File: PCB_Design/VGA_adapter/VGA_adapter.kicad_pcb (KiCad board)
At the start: 2 copper layers, 62.2 x 44.5 mm, 2 parts, among them J1 VGA Output, J2 PIC24 Curiosity Board Adapter

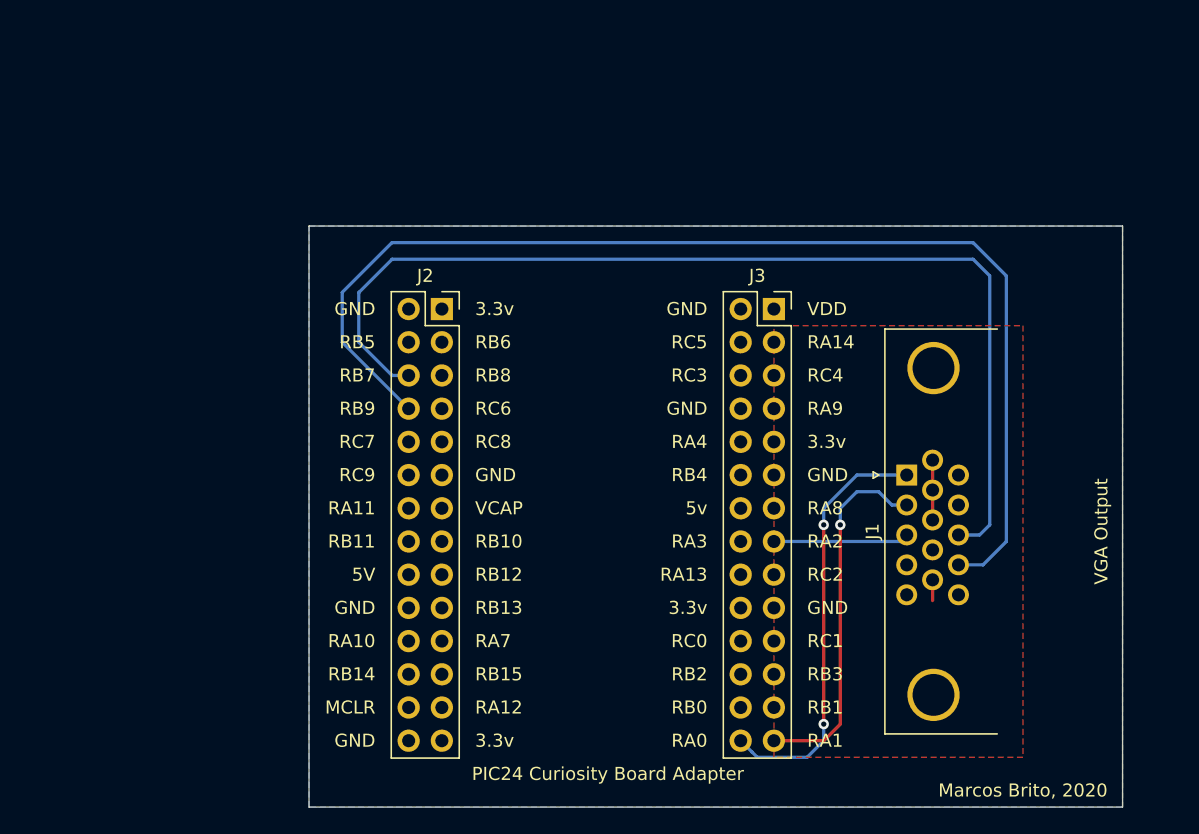
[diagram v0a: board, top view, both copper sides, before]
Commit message: First version of PCB adapter
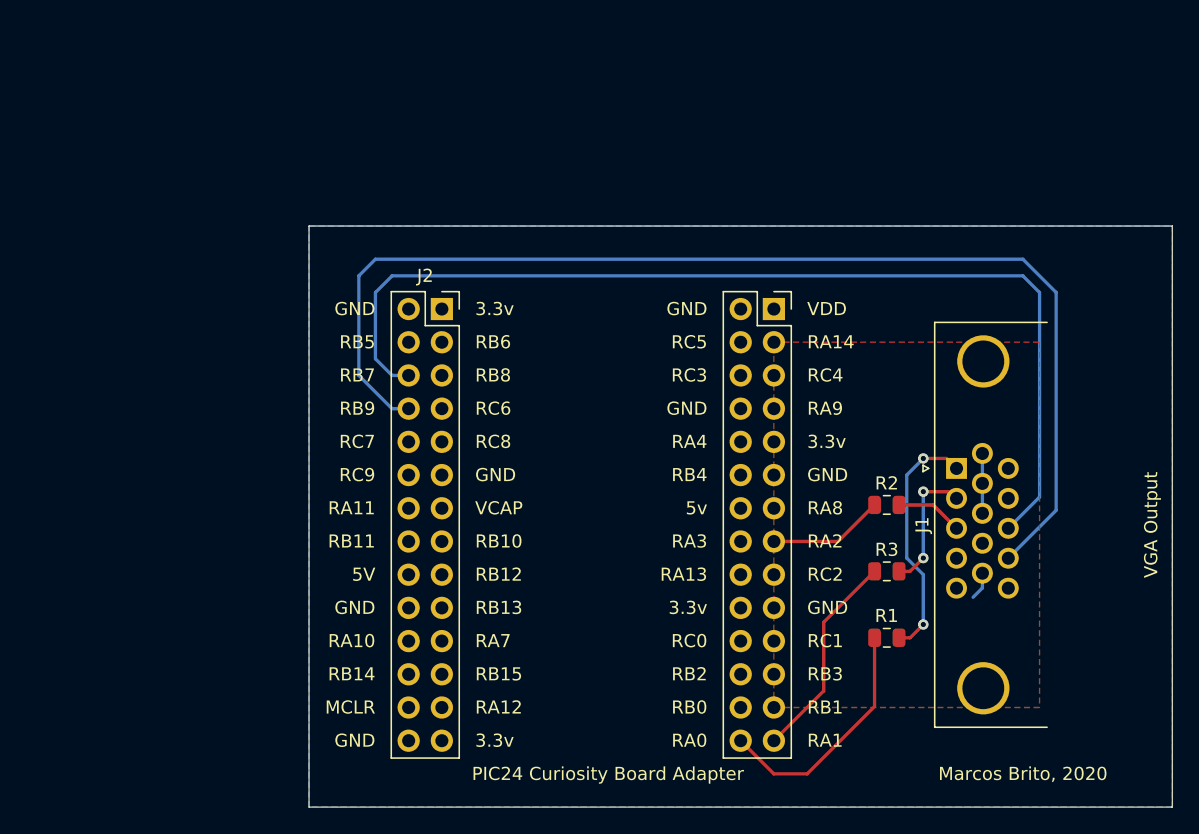
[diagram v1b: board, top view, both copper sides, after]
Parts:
- added R1: 470, Resistor_SMD:R_0805_2012Metric, F.Cu at (171.2, 109.0)
- added R2: 470, Resistor_SMD:R_0805_2012Metric, F.Cu at (171.2, 98.8)
- added R3: 470, Resistor_SMD:R_0805_2012Metric, F.Cu at (171.2, 103.9)
- moved J1 3.84 mm to (176.5, 96.0)
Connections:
- J1 pad 11: Net-(J1-Pad11) -> (no net)
- J2 pad 43: BLUE -> Net-(J2-Pad43)
- J2 pad 55: GREEN -> Net-(J2-Pad55)
- J2 pad 56: RED -> Net-(J2-Pad56)
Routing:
- net Net-(J2-Pad56): track 0.00 -> 18.7 mm
- net GREEN: track 28.1 -> 10.1 mm, vias 1 -> 2
- net Net-(J2-Pad55): track 0.00 -> 16.1 mm
- net RED: track 32.6 -> 18.9 mm
- net Net-(J2-Pad43): track 0.00 -> 8.86 mm
- net BLUE: track 10.4 -> 5.14 mm
- net H_SYNC: track 80.3 -> 79.0 mm
- net GND: track 6.17 -> 6.72 mm
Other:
- board size 62.2 x 44.5 mm -> 66 x 44.5 mm
- board text removed: "J3"

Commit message: PCB_Design: Add resistors to .sch and 3D model for pins
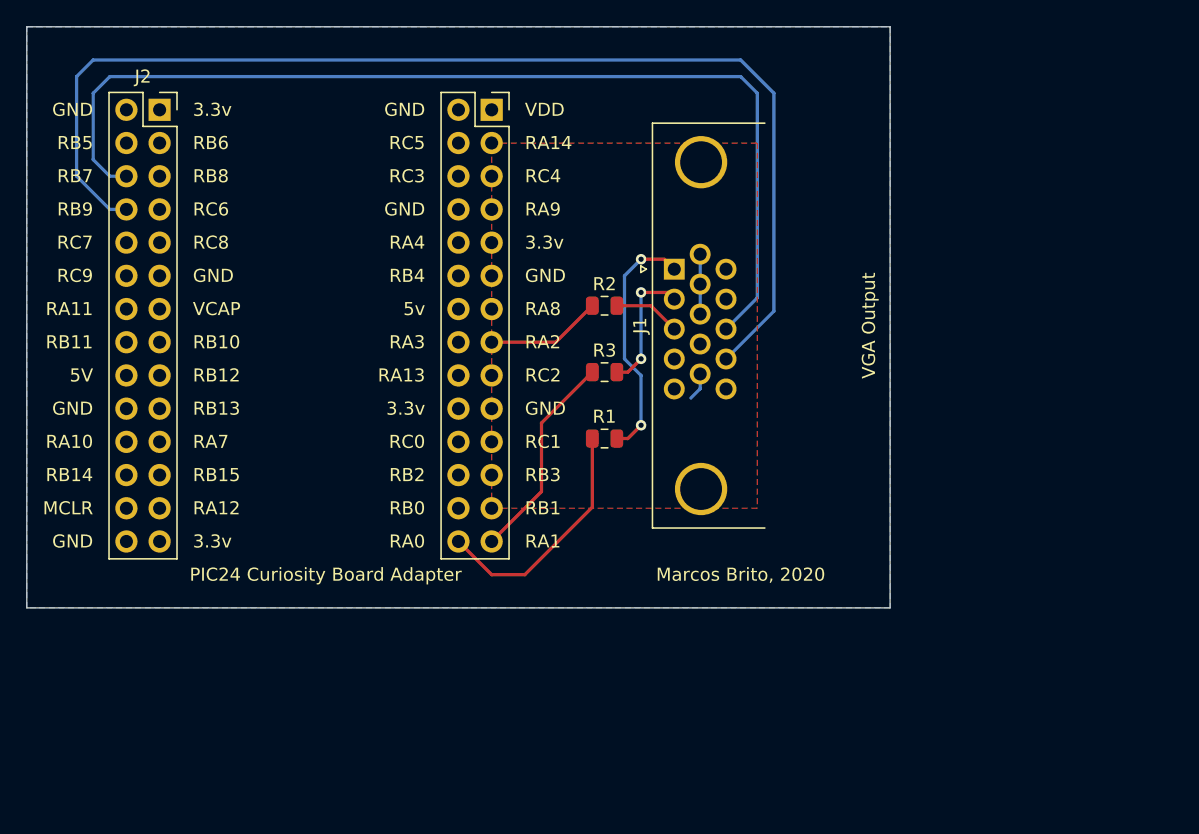
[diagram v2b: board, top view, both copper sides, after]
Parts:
- moved J1 26.4 mm to (154.9, 80.8)
- moved J2 26.4 mm to (113.0, 68.6)
- moved R1 26.4 mm to (149.6, 93.7)
- moved R2 26.4 mm to (149.6, 83.6)
- moved R3 26.4 mm to (149.6, 88.6)
